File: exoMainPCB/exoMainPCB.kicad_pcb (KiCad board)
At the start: 4 copper layers, 105 x 70 mm, 92 parts, among them J1 Conn_02x06_Odd_Even, J10 Conn_01x03_Pin, J11 USB_A, J12 USB_A, J13 USB_A, J14 Screw_Terminal_01x02, J15 Conn_01x03, J16 Conn_01x02, J17 Screw_Terminal_01x02, J2 HDMI_A, J3 USB_A, J4 Conn_01x02, J5 Conn_01x03, J6 Conn_01x03_Pin, J7 Conn_01x02, J8 Screw_Terminal_01x02, J9 Conn_01x12, SW1 SW_SPDT, SW2 SW_Push, SW3 SW_SPDT, U1 MCP2515-I/ST, U14 SI8642ED-B-IS, U15 SN65HVD230D, U17 SM24CANB-02HTG, U2 MCP2515-I/ST, U3 BNO085, U4 SL2.1A, U5 MCP3008, U7 SN65HVD230D, U8 SM24CANB-02HTG, Y1 16 MHz, Y2 16 MHz, Y3 12 MHz, Y4 32.768 kHz

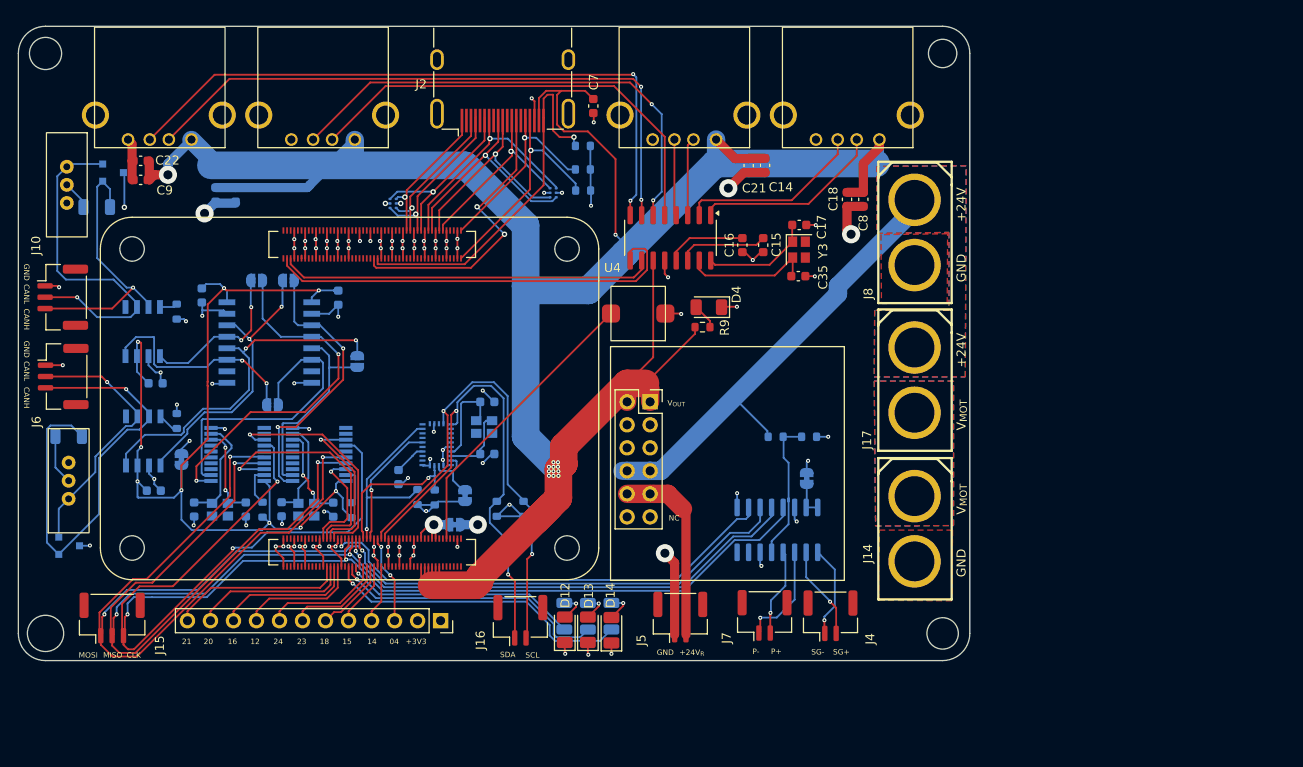
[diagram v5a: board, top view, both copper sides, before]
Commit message: added CAN, HDMI, USB test points, fixed JST connector orientations
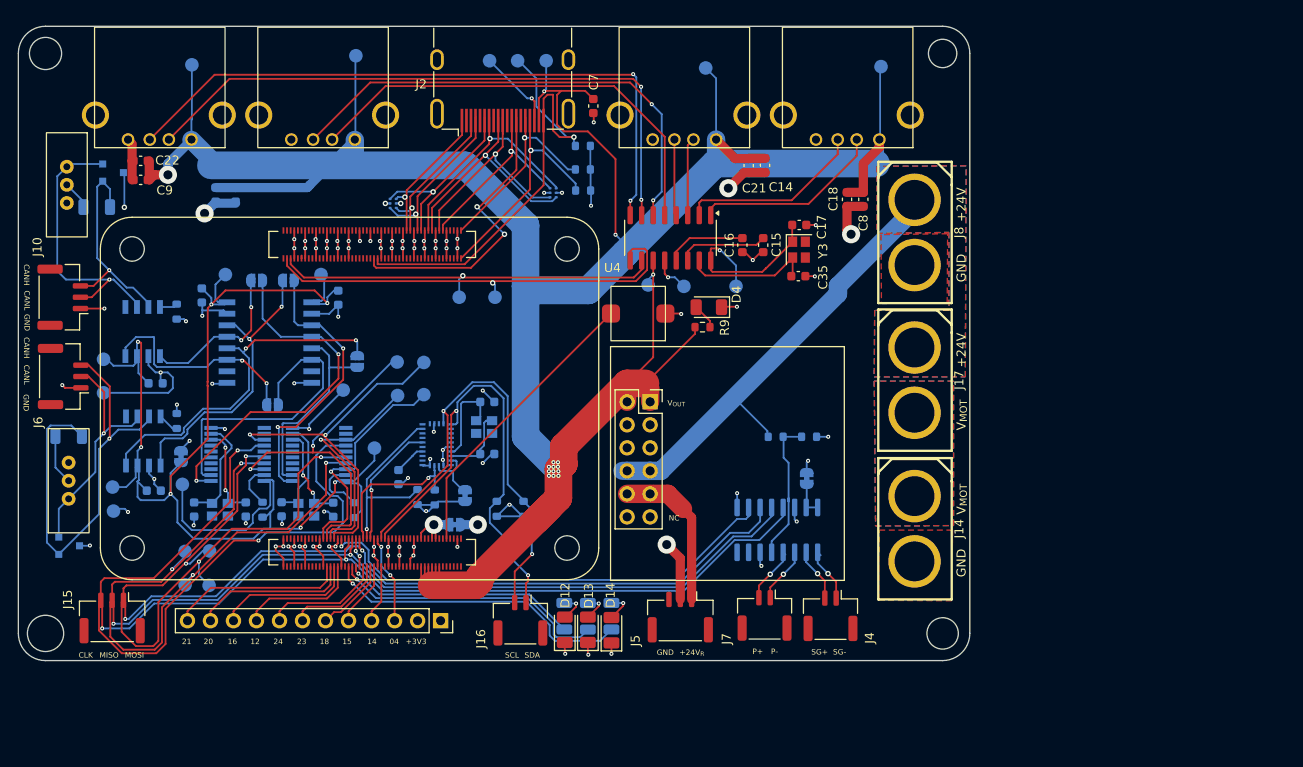
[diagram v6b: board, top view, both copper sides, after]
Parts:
- added TP1: TestPoint, TestPoint:TestPoint_Pad_D1.5mm, B.Cu at (115.5, 29.1)
- added TP10: TestPoint, TestPoint:TestPoint_Pad_D1.5mm, B.Cu at (112.5, 29.1)
- added TP11: TestPoint, TestPoint:TestPoint_Pad_D1.5mm, B.Cu at (70.8, 76.1)
- added TP12: TestPoint, TestPoint:TestPoint_Pad_D1.5mm, B.Cu at (69.8, 62.0)
- added TP13: TestPoint, TestPoint:TestPoint_Pad_D1.5mm, B.Cu at (102.2, 62.3)
- added TP14: TestPoint, TestPoint:TestPoint_Pad_D1.5mm, B.Cu at (78.8, 83.2)
- added TP15: TestPoint, TestPoint:TestPoint_Pad_D1.5mm, B.Cu at (81.5, 83.2)
- added TP16: TestPoint, TestPoint:TestPoint_Pad_D1.5mm, B.Cu at (105.2, 65.9)
- added TP17: TestPoint, TestPoint:TestPoint_Pad_D1.5mm, B.Cu at (105.2, 62.4)
- added TP18: TestPoint, TestPoint:TestPoint_Pad_D1.5mm, B.Cu at (78.8, 86.9)
- added TP19: TestPoint, TestPoint:TestPoint_Pad_D1.5mm, B.Cu at (81.5, 87.0)
- added TP2: TestPoint, TestPoint:TestPoint_Pad_D1.5mm, B.Cu at (139.7, 54.0)
- added TP20: TestPoint, TestPoint:TestPoint_Pad_D1.5mm, B.Cu at (102.3, 66.0)
- added TP21: TestPoint, TestPoint:TestPoint_Pad_D1.5mm, B.Cu at (99.8, 71.8)
- added TP22: TestPoint, TestPoint:TestPoint_Pad_D1.5mm, B.Cu at (78.5, 75.8)
- added TP23: TestPoint, TestPoint:TestPoint_Pad_D1.5mm, B.Cu at (93.8, 52.6)
- added TP24: TestPoint, TestPoint:TestPoint_Pad_D1.5mm, B.Cu at (83.3, 52.6)
- added TP25: TestPoint, TestPoint:TestPoint_Pad_D1.5mm, B.Cu at (69.8, 65.7)
- added TP26: TestPoint, TestPoint:TestPoint_Pad_D1.5mm, B.Cu at (71.0, 78.8)
- added TP27: TestPoint, TestPoint:TestPoint_Pad_D1.5mm, B.Cu at (96.3, 65.4)
- added TP29: TestPoint, TestPoint:TestPoint_Pad_D1.5mm, B.Cu at (109.1, 55.1)
- added TP3: TestPoint, TestPoint:TestPoint_Pad_D1.5mm, B.Cu at (133.9, 54.0)
- added TP30: TestPoint, TestPoint:TestPoint_Pad_D1.5mm, B.Cu at (113.0, 55.1)
- added TP4: TestPoint, TestPoint:TestPoint_Pad_D1.5mm, B.Cu at (129.9, 53.8)
- added TP5: TestPoint, TestPoint:TestPoint_Pad_D1.5mm, B.Cu at (79.6, 29.5)
- added TP6: TestPoint, TestPoint:TestPoint_Pad_D1.5mm, B.Cu at (136.3, 29.9)
- added TP7: TestPoint, TestPoint:TestPoint_Pad_D1.5mm, B.Cu at (97.7, 28.5)
- added TP8: TestPoint, TestPoint:TestPoint_Pad_D1.5mm, B.Cu at (155.7, 29.7)
- added TP9: TestPoint, TestPoint:TestPoint_Pad_D1.5mm, B.Cu at (118.7, 29.1)
- C1, C3, C4: value 22pF -> 22 pF
- C10: value 0.1uF -> 0.1 uF
- C15, C16: value 10uF -> 10 uF
- J5: footprint Connector_JST:JST_GH_BM02B-GHS-TBT_1x02-1MP_P1.25mm_Vertical -> Connector_JST:JST_GH_BM03B-GHS-TBT_1x03-1MP_P1.25mm_Vertical
- moved JP5 0.30 mm to (78.4, 72.8)
- moved R4 0.30 mm to (97.5, 78.7)
- turned J10 to 90 degrees
- turned J15 to 180 degrees
- turned J16 to 180 degrees
- turned J4 to 180 degrees
- turned J5 to 180 degrees
- turned J6 to 90 degrees
- turned J7 to 180 degrees
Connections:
- J5 pad 1: GND -> /V_{RP}
- J5 pad 2: /V_{RP} -> GND
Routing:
- net /+3V3_{CAN}: track 110.2 -> 159.9 mm, vias 9 -> 7
- net +5V: track 273.7 -> 313.0 mm, vias 13 -> 15
- net GND: track 188.3 -> 213.5 mm, vias 99 -> 100
- net /D_{INT1}: track 25.3 -> 39.4 mm, vias 1 -> 2
- net /D_{CS0}: track 11.9 -> 25.6 mm
- net /D_{CS1}: track 26.3 -> 38.0 mm, vias 1 -> 2
- net /D_{HDMI0_HOTPLUG}: track 41.0 -> 52.6 mm
- net /SCK: track 160.7 -> 171.6 mm
- net Net-(U4-XIN): track 12.2 -> 20.6 mm, vias 0 -> 1
- net /D_{INT0}: track 17.6 -> 25.4 mm
- net Net-(J10-Pin_2): track 38.5 -> 31.1 mm
- net /MISO: track 153.1 -> 160.1 mm, vias 4 -> 6
- net Net-(J10-Pin_3): track 30.7 -> 24.0 mm
- net /P_{IN,-}: track 11.7 -> 6.13 mm
- net /SG_{IN,+}: track 10.4 -> 5.90 mm
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
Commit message: fixed pours and added testpoints to last systems
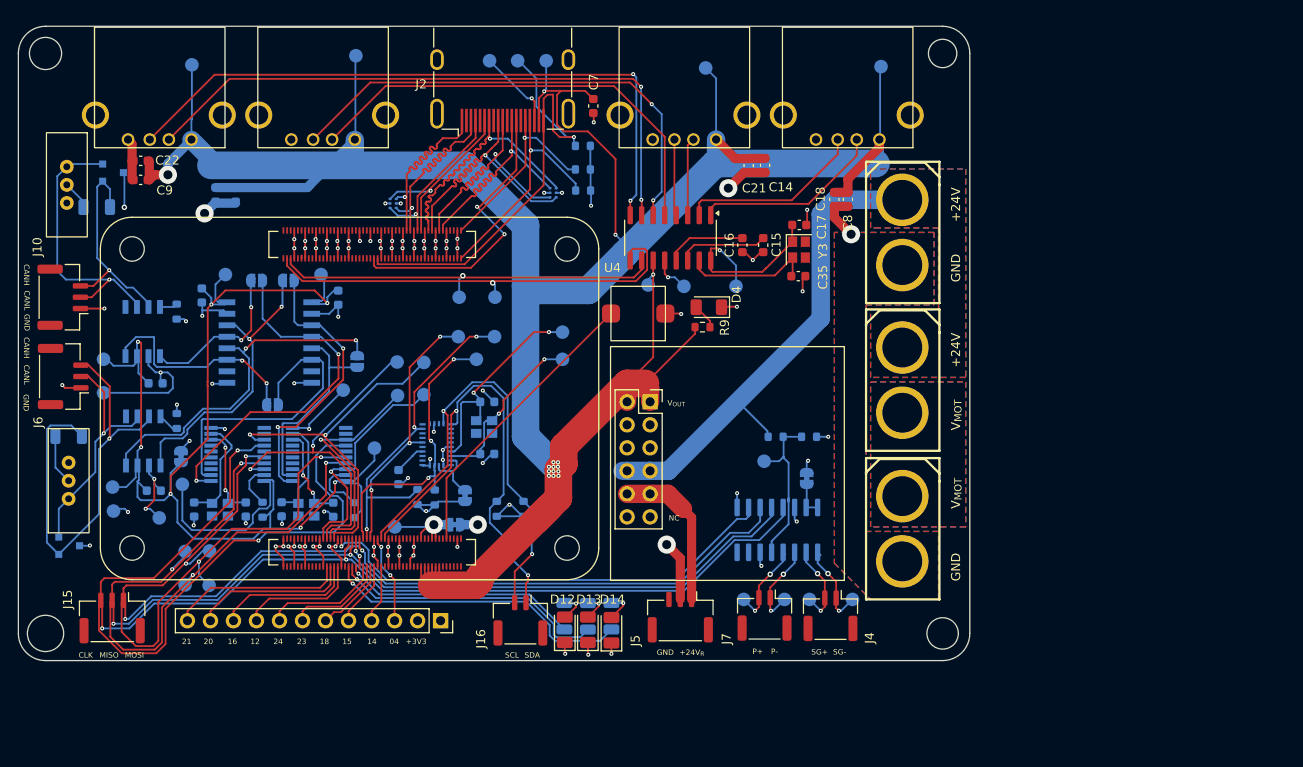
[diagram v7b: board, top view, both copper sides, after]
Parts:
- added BAT_SIG: TestPoint, TestPoint:TestPoint_Pad_D1.5mm, B.Cu at (142.8, 73.2)
- added IM_{BT}: TestPoint, TestPoint:TestPoint_Pad_D1.5mm, B.Cu at (111.0, 62.0)
- added IM_{INT}: TestPoint, TestPoint:TestPoint_Pad_D1.5mm, B.Cu at (113.0, 59.5)
- added IM_{RST}: TestPoint, TestPoint:TestPoint_Pad_D1.5mm, B.Cu at (109.0, 59.5)
- added PR+: TestPoint, TestPoint:TestPoint_Pad_D1.5mm, B.Cu at (140.5, 88.5)
- added PR-: TestPoint, TestPoint:TestPoint_Pad_D1.5mm, B.Cu at (145.0, 88.5)
- added S+: TestPoint, TestPoint:TestPoint_Pad_D1.5mm, B.Cu at (147.8, 88.5)
- added S-: TestPoint, TestPoint:TestPoint_Pad_D1.5mm, B.Cu at (152.5, 88.5)
- added TP28: TestPoint, TestPoint:TestPoint_Pad_D1.5mm, B.Cu at (76.0, 79.5)
- added TP39: TestPoint, TestPoint:TestPoint_Pad_D1.5mm, B.Cu at (120.5, 62.0)
- added TP40: TestPoint, TestPoint:TestPoint_Pad_D1.5mm, B.Cu at (120.5, 59.0)
- added TP41: TestPoint, TestPoint:TestPoint_Pad_D1.5mm, B.Cu at (102.0, 80.5)
- moved C8 1.70 mm to (152.0, 44.4)
- moved C18 1.40 mm to (150.5, 44.4)
- moved J14 1.35 mm to (158.0, 80.7)
- moved J17 1.35 mm to (158.0, 64.3)
- moved J8 1.35 mm to (158.0, 48.0)
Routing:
- net /IMU_{HINT}: track 21.0 -> 37.2 mm, vias 1 -> 3
- net /IMU_{BOOT}: track 16.6 -> 32.3 mm, vias 1 -> 3
- net /IMU_{RST}: track 13.9 -> 29.2 mm, vias 1 -> 3
- net Net-(U3-XOUT32/CLKSEL1): track 10.4 -> 24.3 mm, vias 0 -> 2
- net Net-(U3-XIN32): track 7.94 -> 19.1 mm, vias 0 -> 2
- net GND: track 213.5 -> 220.8 mm, vias 100 -> 101
- net +24V: track 50.1 -> 55.9 mm
- net /D_{HDMI0_TX2_P}: track 16.1 -> 21.2 mm
- net /D_{HDMI0_TX2_N}: track 17.3 -> 22.2 mm
- net /D_{HDMI0_TX0_N}: track 25.6 -> 30.3 mm
- net /D_{HDMI0_TX0_P}: track 25.0 -> 29.4 mm
- net Net-(JP9-A): track 7.30 -> 11.7 mm
- net /D_{HDMI0_CLK_P}: track 23.8 -> 27.9 mm
- net /D_{HDMI0_CLK_N}: track 21.6 -> 25.5 mm
- net /SG_{IN,-}: track 6.36 -> 9.90 mm, vias 1 -> 2
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- added copper zone on B.Cu, net GND

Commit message: generated bom and placements, ordered PCB
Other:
- board text added: "UNTETHERED EXO V1.0"
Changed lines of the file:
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@@
+		)
+	)
+	(gr_text "UNTETHERED EXO\nV1.0"
+		(at 63.5 35.25 90)
+		(layer "F.SilkS")
+		(effects
+			(font
+				(size 0.75 0.75)
+				(thickness 0.1)
+			)
+			(justify bottom)
 		)
 	)
